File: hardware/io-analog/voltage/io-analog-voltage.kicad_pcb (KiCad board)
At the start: 2 copper layers, 60 x 60 mm, 27 parts, among them J1 Analog Extension, J2 Output, J3 Power, U1 TLV2772, U2 TLV2772, U3 LM317T

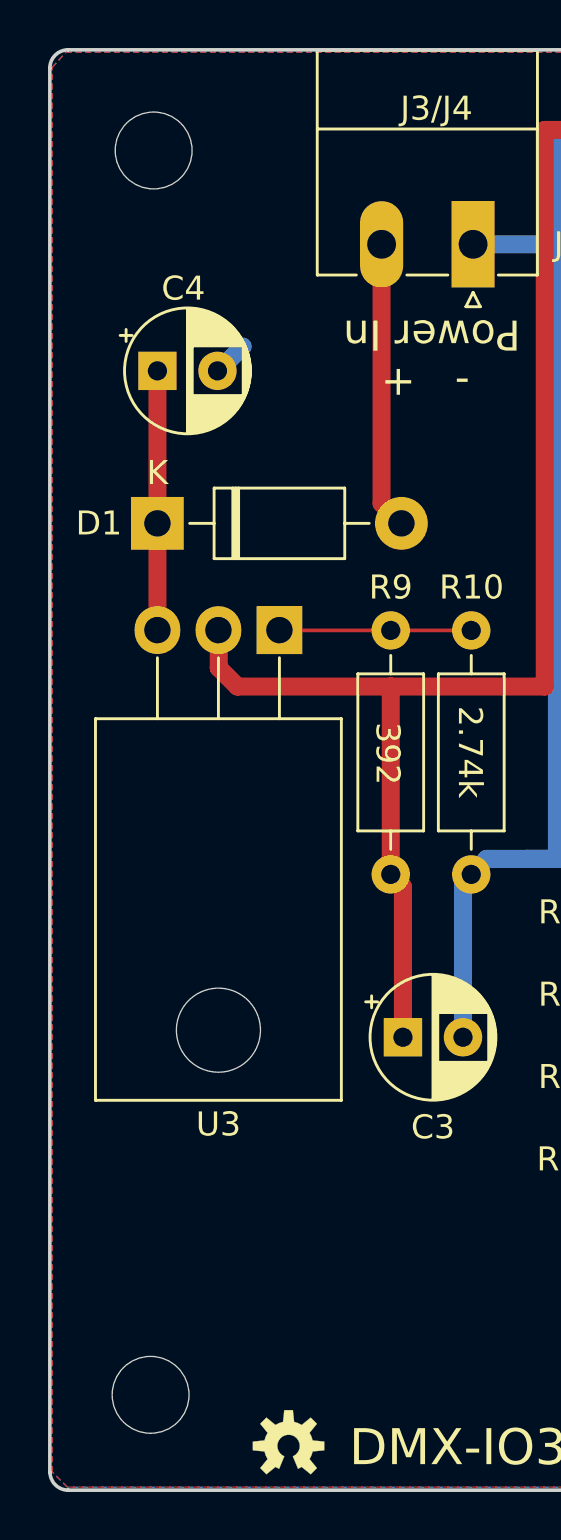
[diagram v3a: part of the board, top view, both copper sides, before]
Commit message: Tweaks boards based on construction notes
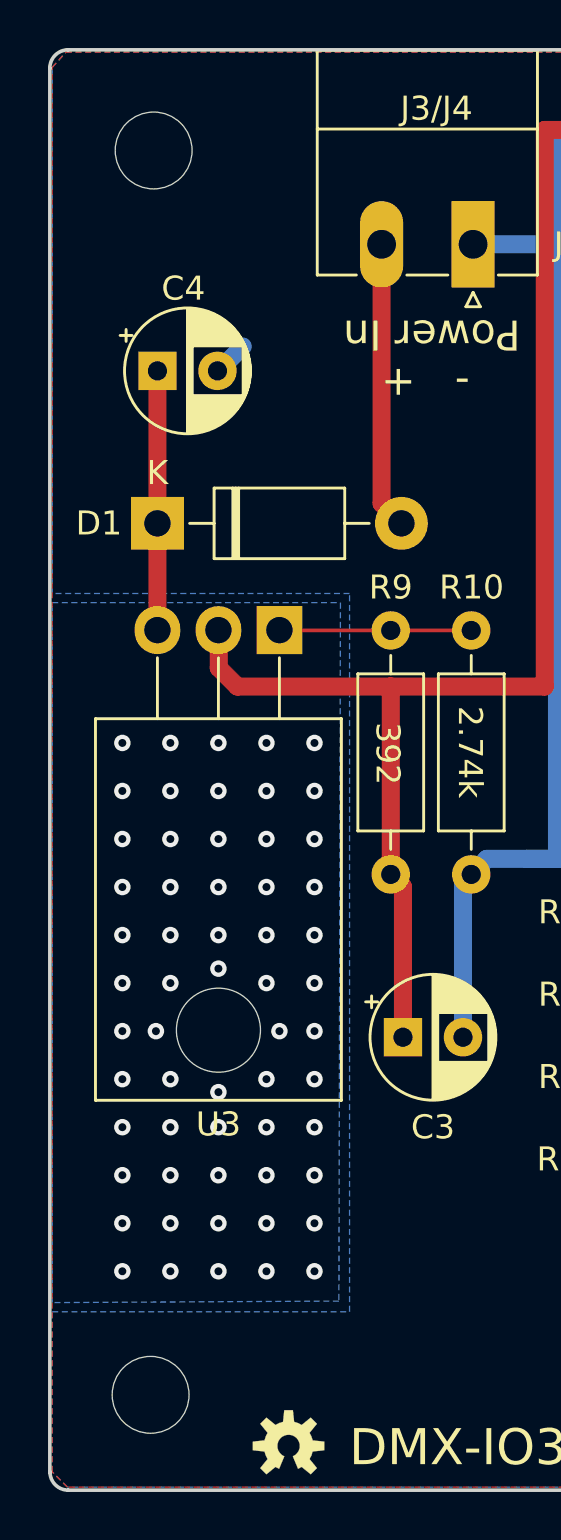
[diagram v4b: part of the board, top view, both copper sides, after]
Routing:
- net Net-(C1-Pad1): vias 0 -> 59
- net (no net): vias 0 -> 1
- added copper zone on B.Cu, net Net-(C1-Pad1)
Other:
- board text added: "DMX-IO3, Rev 1.4 Crazy Giraffe Software"
- board text removed: "DMX-IO3, Rev 1.3 Crazy Giraffe Software"
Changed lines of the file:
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@@
     (thickness 1.6)
     (drawings 27)
-    (tracks 160)
+    (tracks 220)
     (zones 0)
     (modules 27)
@@
   (title_block
     (title "DMX Demonstrator - Analog IO Voltage (DMX-IO3)")
-    (date 2023-09-17)
-    (rev 1.3)
+    (date 2023-12-19)
+    (rev 1.4)
     (company "Crazy Giraffe Software")
     (comment 2 "Designed by: SparkyBobo")
@@
   )
   (layers
-    (0 F.Cu signal)
-    (31 B.Cu signal)
+    (0 F.Cu signal hide)
+    (31 B.Cu signal hide)
     (32 B.Adhes user)
     (33 F.Adhes user)
@@
   (gr_line (start 127.0914 133.7945) (end 185.5114 133.7945) (layer Edge.Cuts) (width 0.15))
   (gr_line (start 126.3294 133.0555) (end 126.3294 74.5795) (layer Edge.Cuts) (width 0.15))
-  (gr_text "DMX-IO3, Rev 1.3\nCrazy Giraffe Software\n\n" (at 147.6375 129.9845) (layer B.SilkS)
+  (gr_text "DMX-IO3, Rev 1.4\nCrazy Giraffe Software\n\n" (at 147.6375 129.9845) (layer B.SilkS)
     (effects (font (size 1 1) (thickness 0.15) italic) (justify mirror))
   )
@@
   (segment (start 146.939 77.1525) (end 161.417 77.1525) (width 0.75) (layer F.Cu) (net 16))
   (segment (start 161.417 77.1525) (end 173.9265 77.1525) (width 0.75) (layer F.Cu) (net 16))
+  (via (at 129.3495 102.6795) (size 0.6858) (drill 0.3302) (layers F.Cu B.Cu) (net 16))
+  (via (at 131.3495 102.6795) (size 0.6858) (drill 0.3302) (layers F.Cu B.Cu) (net 16))
+  (via (at 133.3495 102.6795) (size 0.6858) (drill 0.3302) (layers F.Cu B.Cu) (net 16))
+  (via (at 135.3495 102.6795) (size 0.6858) (drill 0.3302) (layers F.Cu B.Cu) (net 16))
+  (via (at 137.3495 102.6795) (size 0.6858) (drill 0.3302) (layers F.Cu B.Cu) (net 16))
+  (via (at 129.3495 104.6795) (size 0.6858) (drill 0.3302) (layers F.Cu B.Cu) (net 16))
+  (via (at 131.3495 104.6795) (size 0.6858) (drill 0.3302) (layers F.Cu B.Cu) (net 16))
+  (via (at 133.3495 104.6795) (size 0.6858) (drill 0.3302) (layers F.Cu B.Cu) (net 16))
+  (via (at 135.3495 104.6795) (size 0.6858) (drill 0.3302) (layers F.Cu B.Cu) (net 16))
+  (via (at 137.3495 104.6795) (size 0.6858) (drill 0.3302) (layers F.Cu B.Cu) (net 16))
+  (via (at 129.3495 106.6795) (size 0.6858) (drill 0.3302) (layers F.Cu B.Cu) (net 16))
+  (via (at 131.3495 106.6795) (size 0.6858) (drill 0.3302) (layers F.Cu B.Cu) (net 16))
+  (via (at 133.3495 106.6795) (size 0.6858) (drill 0.3302) (layers F.Cu B.Cu) (net 16))
+  (via (at 135.3495 106.6795) (size 0.6858) (drill 0.3302) (layers F.Cu B.Cu) (net 16))
+  (via (at 137.3495 106.6795) (size 0.6858) (drill 0.3302) (layers F.Cu B.Cu) (net 16))
+  (via (at 129.3495 108.6795) (size 0.6858) (drill 0.3302) (layers F.Cu B.Cu) (net 16))
+  (via (at 131.3495 108.6795) (size 0.6858) (drill 0.3302) (layers F.Cu B.Cu) (net 16))
+  (via (at 133.3495 108.6795) (size 0.6858) (drill 0.3302) (layers F.Cu B.Cu) (net 16))
+  (via (at 135.3495 108.6795) (size 0.6858) (drill 0.3302) (layers F.Cu B.Cu) (net 16))
+  (via (at 137.3495 108.6795) (size 0.6858) (drill 0.3302) (layers F.Cu B.Cu) (net 16))
+  (via (at 129.3495 110.6795) (size 0.6858) (drill 0.3302) (layers F.Cu B.Cu) (net 16))
+  (via (at 131.3495 110.6795) (size 0.6858) (drill 0.3302) (layers F.Cu B.Cu) (net 16))
+  (via (at 133.3495 110.6795) (size 0.6858) (drill 0.3302) (layers F.Cu B.Cu) (net 16))
+  (via (at 135.3495 110.6795) (size 0.6858) (drill 0.3302) (layers F.Cu B.Cu) (net 16))
+  (via (at 137.3495 110.6795) (size 0.6858) (drill 0.3302) (layers F.Cu B.Cu) (net 16))
+  (via (at 129.3495 112.6795) (size 0.6858) (drill 0.3302) (layers F.Cu B.Cu) (net 16))
+  (via (at 131.3495 112.6795) (size 0.6858) (drill 0.3302) (layers F.Cu B.Cu) (net 16))
+  (via (at 133.3495 112.0775) (size 0.6858) (drill 0.3302) (layers F.Cu B.Cu) (net 16))
+  (via (at 135.3495 112.6795) (size 0.6858) (drill 0.3302) (layers F.Cu B.Cu) (net 16))
+  (via (at 137.3495 112.6795) (size 0.6858) (drill 0.3302) (layers F.Cu B.Cu) (net 16))
+  (via (at 129.3495 114.6795) (size 0.6858) (drill 0.3302) (layers F.Cu B.Cu) (net 16))
+  (via (at 130.7465 114.681) (size 0.6858) (drill 0.3302) (layers F.Cu B.Cu) (net 16))
+  (via (at 133.3495 114.6795) (size 0.6858) (drill 0.3302) (layers F.Cu B.Cu) (net 0))
+  (via (at 135.89 114.681) (size 0.6858) (drill 0.3302) (layers F.Cu B.Cu) (net 16))
+  (via (at 137.3495 114.6795) (size 0.6858) (drill 0.3302) (layers F.Cu B.Cu) (net 16))
+  (via (at 129.3495 116.6795) (size 0.6858) (drill 0.3302) (layers F.Cu B.Cu) (net 16))
+  (via (at 131.3495 116.6795) (size 0.6858) (drill 0.3302) (layers F.Cu B.Cu) (net 16))
+  (via (at 133.3495 117.221) (size 0.6858) (drill 0.3302) (layers F.Cu B.Cu) (net 16))
+  (via (at 135.3495 116.6795) (size 0.6858) (drill 0.3302) (layers F.Cu B.Cu) (net 16))
+  (via (at 137.3495 116.6795) (size 0.6858) (drill 0.3302) (layers F.Cu B.Cu) (net 16))
+  (via (at 129.3495 118.6795) (size 0.6858) (drill 0.3302) (layers F.Cu B.Cu) (net 16))
+  (via (at 131.3495 118.6795) (size 0.6858) (drill 0.3302) (layers F.Cu B.Cu) (net 16))
+  (via (at 133.3495 118.6795) (size 0.6858) (drill 0.3302) (layers F.Cu B.Cu) (net 16))
+  (via (at 135.3495 118.6795) (size 0.6858) (drill 0.3302) (layers F.Cu B.Cu) (net 16))
+  (via (at 137.3495 118.6795) (size 0.6858) (drill 0.3302) (layers F.Cu B.Cu) (net 16))
+  (via (at 129.3495 120.6795) (size 0.6858) (drill 0.3302) (layers F.Cu B.Cu) (net 16))
+  (via (at 131.3495 120.6795) (size 0.6858) (drill 0.3302) (layers F.Cu B.Cu) (net 16))
+  (via (at 133.3495 120.6795) (size 0.6858) (drill 0.3302) (layers F.Cu B.Cu) (net 16))
+  (via (at 135.3495 120.6795) (size 0.6858) (drill 0.3302) (layers F.Cu B.Cu) (net 16))
+  (via (at 137.3495 120.6795) (size 0.6858) (drill 0.3302) (layers F.Cu B.Cu) (net 16))
+  (via (at 129.3495 122.6795) (size 0.6858) (drill 0.3302) (layers F.Cu B.Cu) (net 16))
+  (via (at 131.3495 122.6795) (size 0.6858) (drill 0.3302) (layers F.Cu B.Cu) (net 16))
+  (via (at 133.3495 122.6795) (size 0.6858) (drill 0.3302) (layers F.Cu B.Cu) (net 16))
+  (via (at 135.3495 122.6795) (size 0.6858) (drill 0.3302) (layers F.Cu B.Cu) (net 16))
+  (via (at 137.3495 122.6795) (size 0.6858) (drill 0.3302) (layers F.Cu B.Cu) (net 16))
+  (via (at 129.3495 124.6795) (size 0.6858) (drill 0.3302) (layers F.Cu B.Cu) (net 16))
+  (via (at 131.3495 124.6795) (size 0.6858) (drill 0.3302) (layers F.Cu B.Cu) (net 16))
+  (via (at 133.3495 124.6795) (size 0.6858) (drill 0.3302) (layers F.Cu B.Cu) (net 16))
+  (via (at 135.3495 124.6795) (size 0.6858) (drill 0.3302) (layers F.Cu B.Cu) (net 16))
+  (via (at 137.3495 124.6795) (size 0.6858) (drill 0.3302) (layers F.Cu B.Cu) (net 16))
   (segment (start 130.81 87.1855) (end 130.81 93.5355) (width 0.75) (layer F.Cu) (net 17))
   (segment (start 130.81 97.9805) (end 130.8227 97.9932) (width 0.75) (layer F.Cu) (net 17))
@@
     (polygon
       (pts
-        (xy 186.2455 132.9055) (xy 185.4835 133.6675) (xy 127.0635 133.6675) (xy 126.4285 133.0325) (xy 126.4285 74.549)
-        (xy 127 73.914) (xy 185.547 73.914) (xy 186.2455 74.549)
+        (xy 186.2455 132.9055) (xy 185.4835 133.6675) (xy 127.0635 133.6675) (xy 126.4285 133.0325) (xy 126.4285 126.365)
+        (xy 138.811 126.365) (xy 138.811 96.4565) (xy 126.4285 96.4565) (xy 126.4285 74.549) (xy 127 73.914)
+        (xy 185.547 73.914) (xy 186.2455 74.549)
       )
     )
   )
-  (zone (net 0) (net_name "") (layer B.Cu) (hatch edge 0.508)
+  (zone (net 16) (net_name "Net-(C1-Pad1)") (layer B.Cu) (hatch edge 0.508)
     (connect_pads (clearance 0.508))
     (min_thickness 0.254)
-    (keepout (tracks not_allowed) (vias not_allowed) (copperpour not_allowed))
-    (fill (arc_segments 16) (thermal_gap 0.508) (thermal_bridge_width 0.508))
+    (fill yes (arc_segments 16) (thermal_gap 0.508) (thermal_bridge_width 0.508))
     (polygon
       (pts
-        (xy 129.6035 111.064394) (xy 137.0965 111.064394) (xy 137.0965 118.11) (xy 129.6035 118.11)
+        (xy 126.4285 96.8375) (xy 138.43 96.8375) (xy 138.3665 125.9205) (xy 126.4285 125.984)
       )
     )

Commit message: Remove non io-analog files. Rebrand.
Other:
- board text added: "DMX-IO3, Rev 1.4 Sparky Bobo Designs"
- board text removed: "DMX-IO3, Rev 1.4 Crazy Giraffe Software"
